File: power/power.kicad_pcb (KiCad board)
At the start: 2 copper layers, 75 x 56 mm, 24 parts, among them J1 GPIO, J2 PWM, J3 Conn_01x16, J4 JP_EXT, Q1 D15P05, U1 XL4015

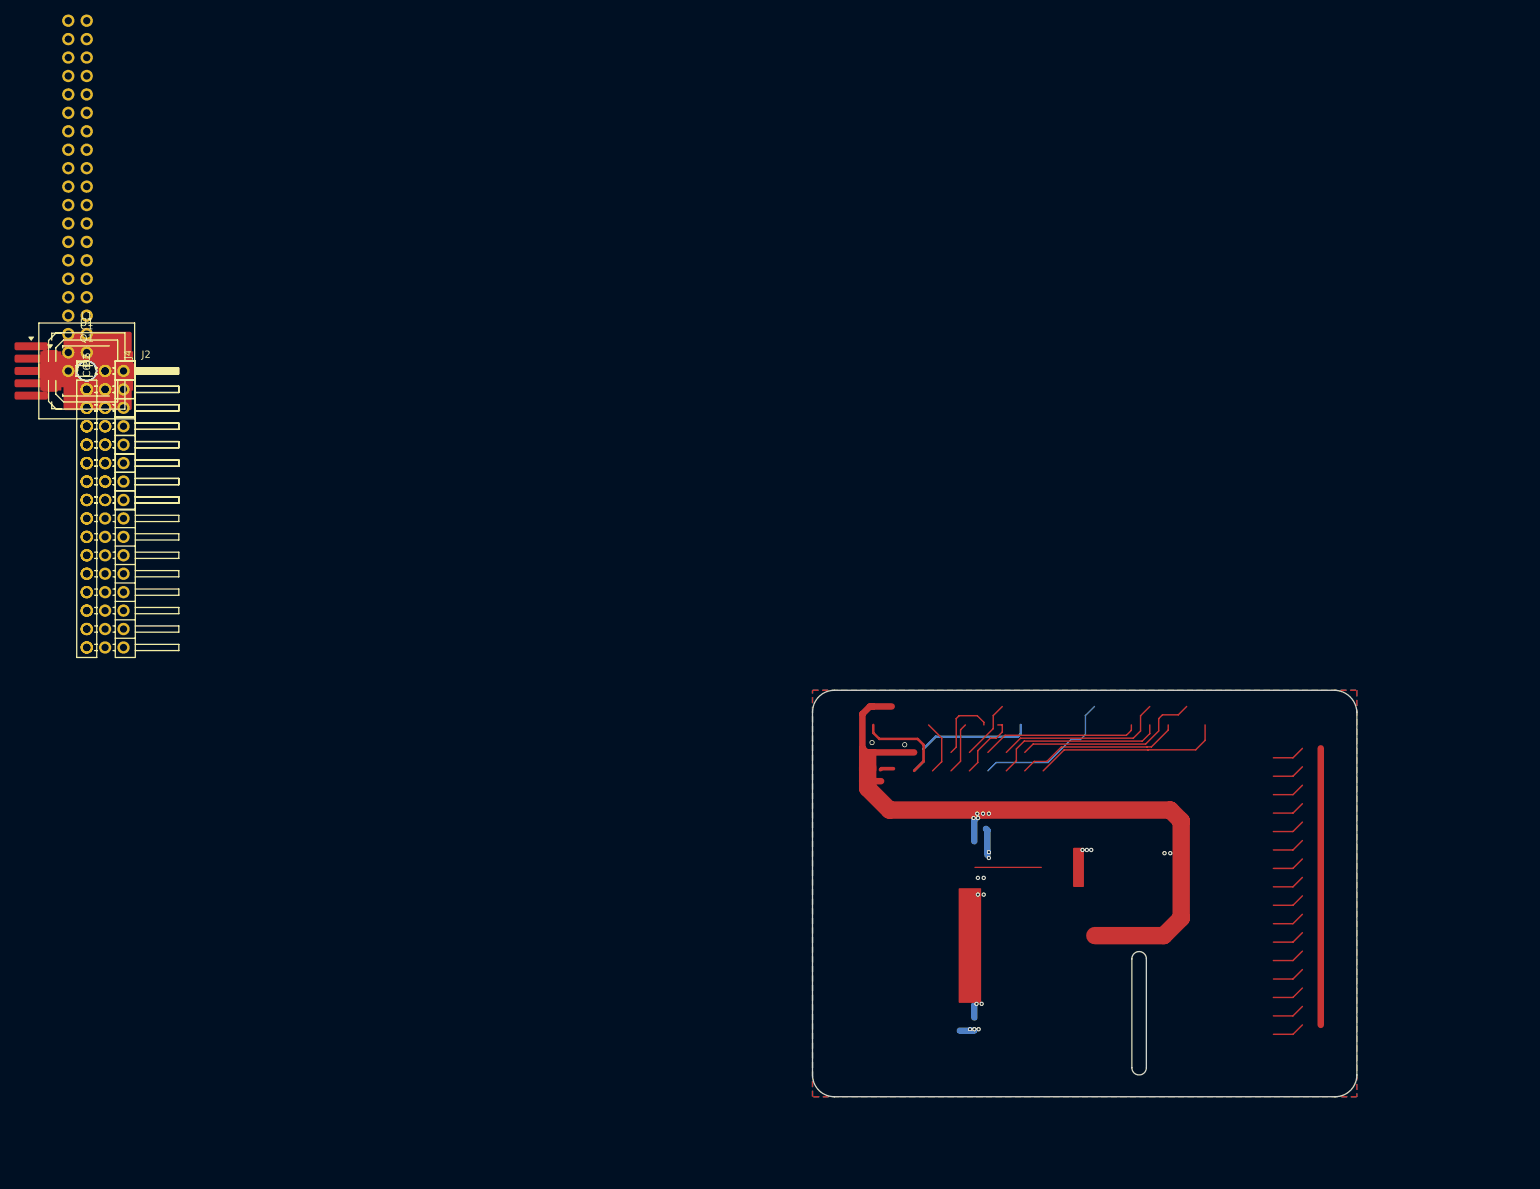
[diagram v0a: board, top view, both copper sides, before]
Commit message: manual downgrade to KiCAD 10.0
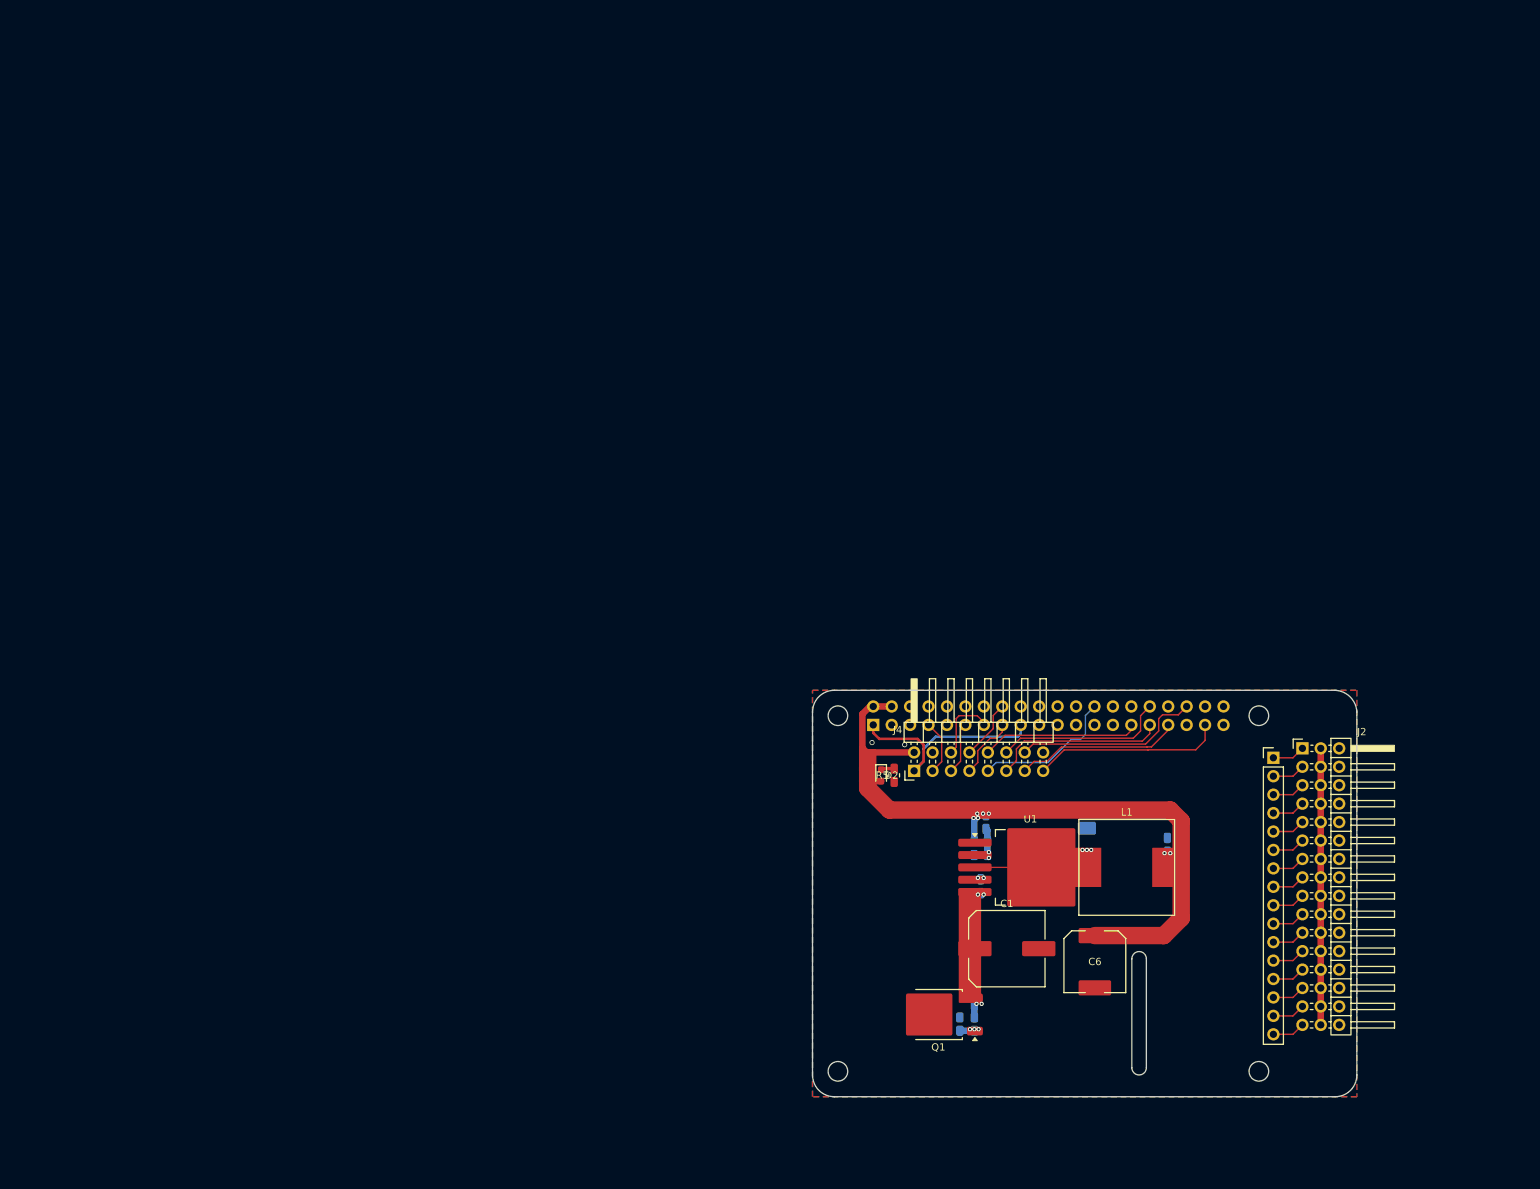
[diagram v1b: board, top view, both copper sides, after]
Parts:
- moved MH4 188.1 mm to (161.5, 96.5)
- moved J2 175.4 mm to (167.5, 52.0)
- moved J3 172.0 mm to (163.5, 53.3)
- moved MH2 168.3 mm to (161.5, 47.5)
- moved C4 162.6 mm to (148.9, 65.3), turned to 90 degrees
- moved C6 161.0 mm to (138.9, 81.4), turned to -90 degrees
- moved L1 158.8 mm to (143.3, 68.4)
- moved D1 152.4 mm to (137.8, 65.0), turned to 90 degrees
- moved R4 151.8 mm to (122.3, 90.0), turned to -90 degrees
- moved R3 150.2 mm to (120.3, 90.0), turned to 90 degrees
- moved C2 149.7 mm to (122.3, 86.4), turned to 90 degrees
- moved C1 149.7 mm to (126.8, 79.6)
- moved Q1 147.1 mm to (117.3, 88.7), turned to 180 degrees
- moved U1 146.9 mm to (130.0, 68.4)
- moved C3 142.2 mm to (123.2, 71.0), turned to 90 degrees
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
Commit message: move buzzer to power board
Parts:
- added BZ1: Buzzer, Buzzer_Beeper:MagneticBuzzer_PUI_AT-0927-TT-6-R, F.Cu at (188.3, 52.2)
- added D3: 1N4148W, Diode_SMD:D_SOD-123, F.Cu at (187.9, 59.1)
- added Q2: SS8050, Package_TO_SOT_SMD:SOT-23, F.Cu at (193.2, 59.7)
- added R6: 1KΩ (1001) ±1%, Resistor_SMD:R_0402_1005Metric, F.Cu at (197.0, 47.9)

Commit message: add buzzer bridged with jumper
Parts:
- added JP1: JP_BUZZ_PWM, Connector_PinHeader_2.54mm:PinHeader_1x02_P2.54mm_Vertical, F.Cu at (153.2, 53.4)
- moved BZ1 51.8 mm to (136.6, 55.6)
- moved Q2 46.7 mm to (146.8, 54.7), turned to 180 degrees
- moved R6 45.4 mm to (152.3, 55.8)
- moved D3 43.3 mm to (144.6, 57.8), turned to 90 degrees
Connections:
- R6 pad 2: /GPIO12/PWM0 -> /Buzzer/PWM
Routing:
- net /GPIO12/PWM0: track 23.6 -> 32.5 mm
- net Net-(BZ1--): track 0.00 -> 6.09 mm
- net +5V: track 97.5 -> 102.5 mm
- net Net-(Q2-B): track 0.00 -> 4.11 mm
- net /Buzzer/PWM: track 0.00 -> 2.56 mm

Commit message: rotate resistor
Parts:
- turned R2 to 180 degrees
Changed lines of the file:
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@@
 	(footprint "Resistor_SMD:R_0805_2012Metric"
 		(layer "B.Cu")
-		(at 123.1875 66.7)
+		(at 123.1875 66.7 180)
 		(descr "Resistor SMD 0805 (2012 Metric), square (rectangular) end terminal, IPC-7351 nominal, (Body size source: IPC-SM-782 page 72, https://www.pcb-3d.com/wordpress/wp-content/uploads/ipc-sm-782a_amendment_1_and_2.pdf)")
 		(tags "resistor")
 		(property "Reference" "R2"
-			(at 0 1.65 180)
+			(at 0 1.65 0)
 			(layer "B.SilkS")
 			(effects
@@
 		)
 		(property "Value" "3.3KΩ (3301) ±1%"
-			(at 5.5875 0 180)
+			(at 5.5875 0 0)
 			(layer "B.Fab")
 			(effects
@@
 		)
 		(property "Datasheet" ""
-			(at 0 0 180)
+			(at 0 0 0)
 			(layer "B.Fab")
 			(hide yes)
@@
 		)
 		(property "Description" "Resistor"
-			(at 0 0 180)
+			(at 0 0 0)
 			(layer "B.Fab")
 			(hide yes)
@@
 		(duplicate_pad_numbers_are_jumpers no)
 		(fp_line
+			(start -0.227064 0.735)
+			(end 0.227064 0.735)
+			(stroke
+				(width 0.12)
+				(type solid)
+			)
+			(layer "B.SilkS")
+		)
+		(fp_line
 			(start -0.227064 -0.735)
 			(end 0.227064 -0.735)
-			(stroke
-				(width 0.12)
-				(type solid)
-			)
-			(layer "B.SilkS")
-		)
-		(fp_line
-			(start -0.227064 0.735)
-			(end 0.227064 0.735)
 			(stroke
 				(width 0.12)
@@
 		)
 		(pad "1" smd roundrect
-			(at -0.9125 0 180)
+			(at -0.9125 0)
 			(size 1.025 1.4)
 			(layers "B.Cu" "B.Mask" "B.Paste")
@@
 		)
 		(pad "2" smd roundrect
-			(at 0.9125 0 180)
+			(at 0.9125 0)
 			(size 1.025 1.4)
 			(layers "B.Cu" "B.Mask" "B.Paste")
@@
 	)
 	(segment
-		(start 126.7 52.56)
-		(end 128.66 50.6)
-		(width 0.2)
-		(layer "F.Cu")
-		(net "/GPIO12{slash}PWM0")
-	)
-	(segment
-		(start 145.2 49.6)
-		(end 145.2 47.5)
-		(width 0.2)
-		(layer "F.Cu")
-		(net "/GPIO12{slash}PWM0")
-	)
-	(segment
-		(start 144.2 50.6)
-		(end 145.2 49.6)
-		(width 0.2)
-		(layer "F.Cu")
-		(net "/GPIO12{slash}PWM0")
-	)
-	(segment
-		(start 145.2 47.5)
-		(end 146.47 46.23)
-		(width 0.2)
-		(layer "F.Cu")
-		(net "/GPIO12{slash}PWM0")
-	)
-	(segment
-		(start 128.66 50.6)
-		(end 144.2 50.6)
-		(width 0.2)
-		(layer "F.Cu")
-		(net "/GPIO12{slash}PWM0")
-	)
-	(segment
-		(start 147.7 47.46)
-		(end 147.7 50.44)
-		(width 0.2)
-		(layer "B.Cu")
-		(net "/GPIO12{slash}PWM0")
-	)
-	(segment
-		(start 146.47 46.23)
-		(end 147.7 47.46)
-		(width 0.2)
-		(layer "B.Cu")
-		(net "/GPIO12{slash}PWM0")
-	)
-	(segment
-		(start 147.7 50.44)
-		(end 150.66 53.4)
-		(width 0.2)
-		(layer "B.Cu")
-		(net "/GPIO12{slash}PWM0")
+		(start 153.2 55.41)
+		(end 153.2 53.4)
+		(width 0.2)
+		(layer "F.Cu")
+		(net "/Buzzer/PWM")
+	)
+	(segment
+		(start 152.81 55.8)
+		(end 153.2 55.41)
+		(width 0.2)
+		(layer "F.Cu")
+		(net "/Buzzer/PWM")
 	)
 	(segment
@@
 		(layer "F.Cu")
 		(net "/GPIO6")
+	)
+	(segment
+		(start 126.7 52.56)
+		(end 128.66 50.6)
+		(width 0.2)
+		(layer "F.Cu")
+		(net "/GPIO12{slash}PWM0")
+	)
+	(segment
+		(start 145.2 49.6)
+		(end 145.2 47.5)
+		(width 0.2)
+		(layer "F.Cu")
+		(net "/GPIO12{slash}PWM0")
+	)
+	(segment
+		(start 144.2 50.6)
+		(end 145.2 49.6)
+		(width 0.2)
+		(layer "F.Cu")
+		(net "/GPIO12{slash}PWM0")
+	)
+	(segment
+		(start 145.2 47.5)
+		(end 146.47 46.23)
+		(width 0.2)
+		(layer "F.Cu")
+		(net "/GPIO12{slash}PWM0")
+	)
+	(segment
+		(start 128.66 50.6)
+		(end 144.2 50.6)
+		(width 0.2)
+		(layer "F.Cu")
+		(net "/GPIO12{slash}PWM0")
+	)
+	(segment
+		(start 147.7 47.46)
+		(end 147.7 50.44)
+		(width 0.2)
+		(layer "B.Cu")
+		(net "/GPIO12{slash}PWM0")
+	)
+	(segment
+		(start 146.47 46.23)
+		(end 147.7 47.46)
+		(width 0.2)
+		(layer "B.Cu")
+		(net "/GPIO12{slash}PWM0")
+	)
+	(segment
+		(start 147.7 50.44)
+		(end 150.66 53.4)
+		(width 0.2)
+		(layer "B.Cu")
+		(net "/GPIO12{slash}PWM0")
 	)
 	(segment
@@
 		(net "Net-(D2-K)")
 	)
-	(segment
-		(start 153.2 55.41)
-		(end 153.2 53.4)
-		(width 0.2)
-		(layer "F.Cu")
-		(net "/Buzzer/PWM")
-	)
-	(segment
-		(start 152.81 55.8)
-		(end 153.2 55.41)
-		(width 0.2)
-		(layer "F.Cu")
-		(net "/Buzzer/PWM")
-	)
 	(zone

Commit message: update footprints from library
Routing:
- net /GPIO13/PWM1: track 22.8 -> 22.1 mm
- net /GPIO22: track 9.30 -> 8.68 mm

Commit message: lots of changes
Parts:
- added C10: 1.0uF (105) 10% 25V, Capacitor_SMD:C_0402_1005Metric, F.Cu at (125.5, 88.5)
- added C11: 330nF (334) 10% 50V, Capacitor_SMD:C_0805_2012Metric, F.Cu at (118.3, 94.7)
- added C12: 100nF(104) 10% 50V, Capacitor_SMD:C_0805_2012Metric, F.Cu at (122.4, 91.7)
- added C7: 1.0uF (105) 10% 25V, Capacitor_SMD:C_0402_1005Metric, F.Cu at (119.6, 86.5)
- added C8: 22uF (226) 20% 6.3V, Capacitor_SMD:C_0603_1608Metric, F.Cu at (113.8, 92.5)
- added C9: 100nF (104) 10% 16V, Capacitor_SMD:C_0402_1005Metric, F.Cu at (126.5, 88.5)
- added J5: JP_VOLTS, Connector_PinSocket_2.54mm:PinSocket_1x02_P2.54mm_Vertical, B.Cu at (114.6, 90.0)
- added R7: 1KΩ (1001) ±1%, Resistor_SMD:R_0805_2012Metric, F.Cu at (112.5, 84.5)
- added R8: 4.7KΩ (4701) ±1%, Resistor_SMD:R_0805_2012Metric, F.Cu at (116.0, 84.5)
- added U2: REF5050IDGK, Package_SO:VSSOP-8_3x3mm_P0.65mm, F.Cu at (121.9, 88.8)
- added U3: L78L06_SOT89, Package_TO_SOT_SMD:SOT-89-3, F.Cu at (121.8, 95.7)
- C2, C3, C4, C5, D1, R1, R2, R3, R4: moved to F.Cu
- J2: value PWM -> PWM_OUT
- J3: value Conn_01x16 -> PWM_IN; footprint Connector_PinHeader_2.54mm:PinHeader_1x16_P2.54mm_Vertical -> Connector_PinSocket_2.54mm:PinSocket_1x16_P2.54mm_Vertical; moved to B.Cu
- J4: footprint Connector_PinHeader_2.54mm:PinHeader_2x08_P2.54mm_Horizontal -> Connector_PinHeader_2.54mm:PinHeader_2x08_P2.54mm_Vertical
- moved D1 22.8 mm to (115.9, 71.2), turned to -90 degrees
- moved C4 17.1 mm to (135.6, 76.0), turned to 180 degrees
- moved C2 11.6 mm to (119.5, 75.1), turned to 180 degrees
- moved Q1 9.67 mm to (113.0, 80.0)
- moved R1 6.86 mm to (116.9, 62.1), turned to -90 degrees
- moved R4 6.25 mm to (119.3, 84.5), turned to 0 degrees
- moved R6 5.89 mm to (146.5, 56.8), turned to -90 degrees
- moved C5 5.06 mm to (118.8, 62.0)
- moved JP1 4.93 mm to (149.0, 56.0), turned to 180 degrees
- moved R3 4.65 mm to (122.7, 86.0), turned to 0 degrees
- moved C3 4.49 mm to (118.7, 71.0)
- moved R2 4.48 mm to (118.8, 65.8), turned to 90 degrees
- moved Q2 1.67 mm to (145.3, 54.0)
- moved D3 0.40 mm to (144.6, 58.2)
- moved L1 0.10 mm to (143.3, 68.3)
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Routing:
- net /VIN: track 1.74 -> 29.6 mm, vias 4 -> 8
- net +5V: track 102.1 -> 82.0 mm, vias 7 -> 0
- net +6V: track 0.00 -> 9.70 mm
- net /VREF: track 0.00 -> 8.89 mm
- net /GPIO14/TXD0: track 0.00 -> 7.63 mm
- net Net-(D1-K): track 9.15 -> 16.3 mm, vias 3 -> 0
- net /BATT_VDIV: track 0.00 -> 4.57 mm
- net Net-(Q1-G): track 1.99 -> 5.83 mm, vias 3 -> 0
- net Net-(U1-VC): track 0.00 -> 3.70 mm, vias 2 -> 0
- net Net-(U1-FB): track 3.68 -> 0.02 mm, vias 2 -> 10
- net Net-(Q2-B): track 3.90 -> 1.42 mm
- net /GPIO7/SPI0.CE1: track 19.9 -> 21.0 mm
- net Net-(U2-Trim/NR): track 0.00 -> 1.04 mm
- net Net-(BZ1--): track 5.69 -> 6.61 mm
- net /GPIO12/PWM0: track 32.5 -> 31.9 mm
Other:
- board text added: "+"
- board text added: "-"
- board text added: "BATT_VDIV"
- board text added: "PWM0"
- board text added: "PWM15"
- board text added: "VREF"
- board text added: "closed = Buzzer open = PWM0"

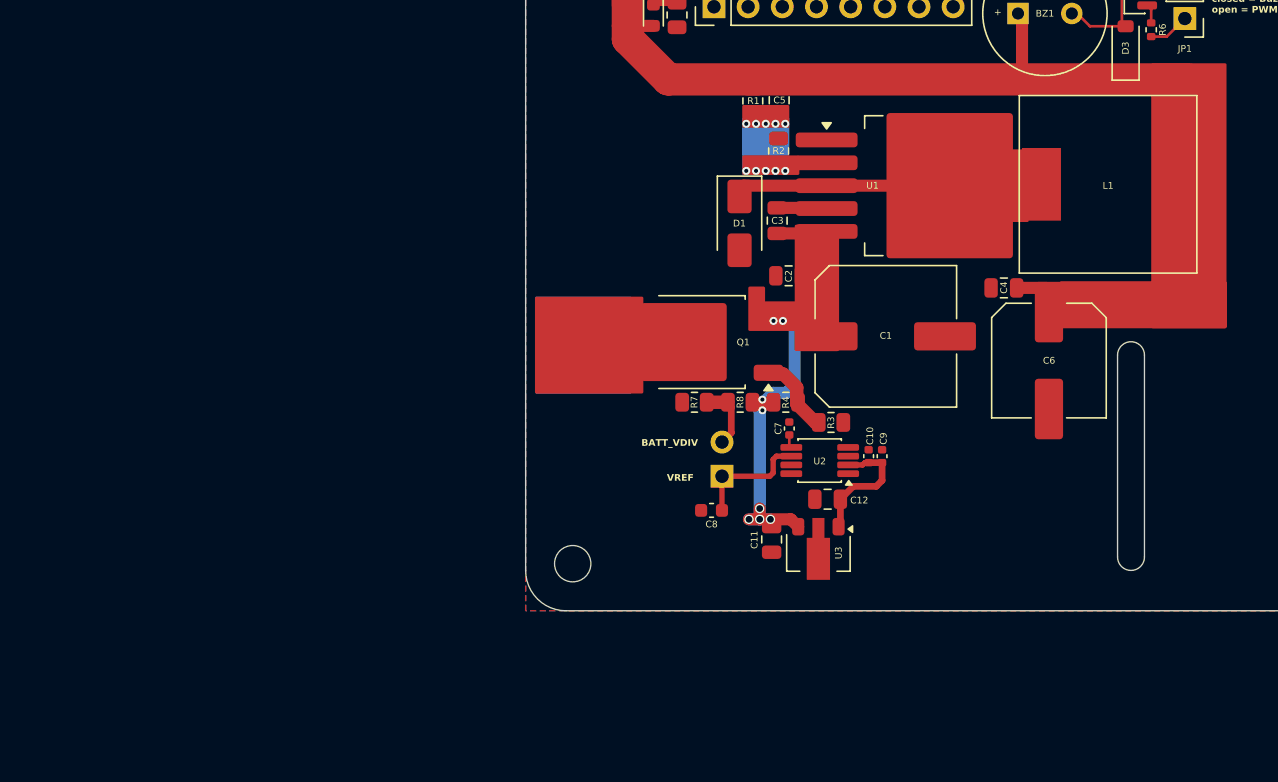
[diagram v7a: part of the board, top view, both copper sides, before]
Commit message: initial TPS56A37 DCDC attempt
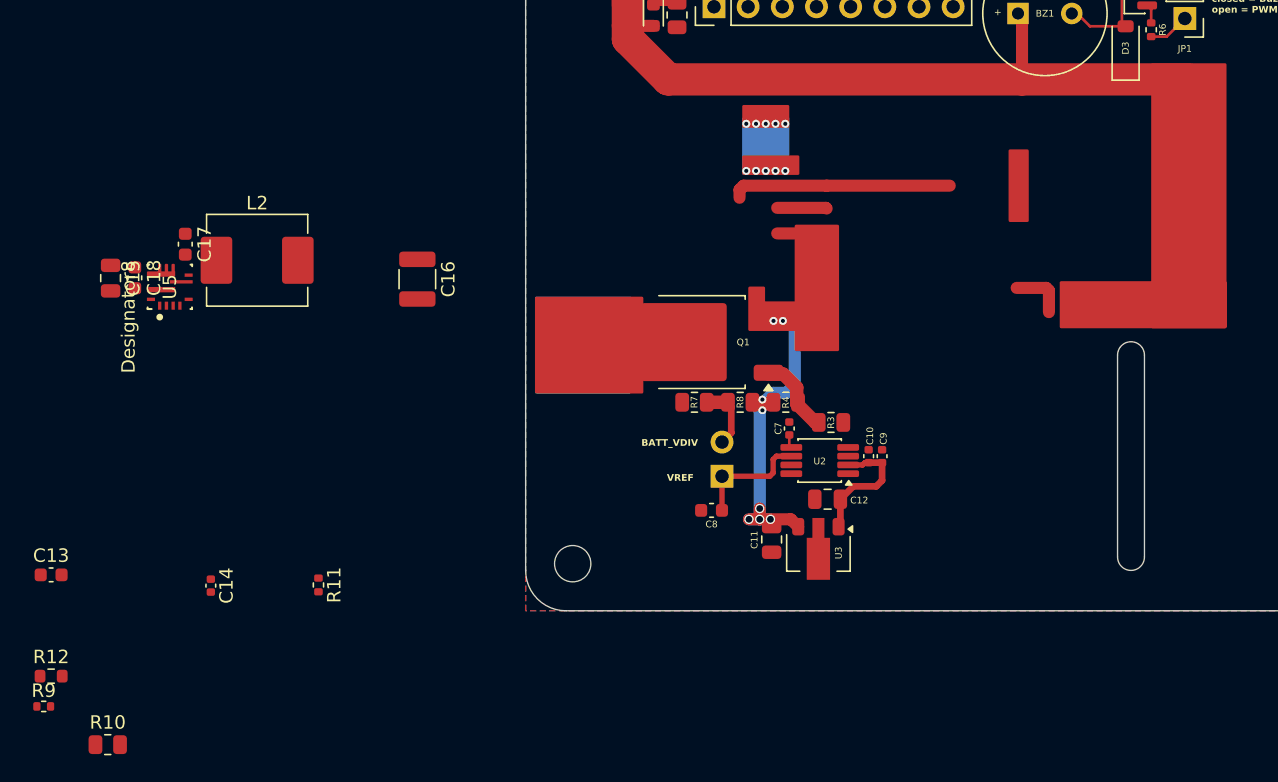
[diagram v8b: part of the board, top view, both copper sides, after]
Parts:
- removed C1: 220uF/50V, Capacitor_SMD:C_Elec_10x10.2
- removed C2, C3, C4: 1uF (105) 10% 50V, Capacitor_SMD:C_0805_2012Metric
- removed C5: 33nF (333) 10% 50V, Capacitor_SMD:C_0805_2012Metric
- removed C6: 470uF/16V, Capacitor_SMD:C_Elec_8x10.2
- removed D1: SS54, Diode_SMD:D_SMA
- removed L1: 47uH, Inductor_SMD:L_Neosid_SM-NE127
- removed R1: 10KΩ (1002) ±1%, Resistor_SMD:R_0805_2012Metric
- removed R2: 3.3KΩ (3301) ±1%, Resistor_SMD:R_0805_2012Metric
- removed U1: XL4015, Package_TO_SOT_SMD:TO-263-5_TabPin3
- added C13: 150pF / 25V, Capacitor_SMD:C_0603_1608Metric, F.Cu at (64.7, 97.3)
- added C14: 22nF (105) 10% 16V, Capacitor_SMD:C_0402_1005Metric, F.Cu at (76.6, 98.1)
- added C15: 10uF 10% 35V, Capacitor_SMD:C_0805_2012Metric, F.Cu at (69.1, 75.3)
- added C16: 22uF 10% 16V, Capacitor_SMD:C_1210_3225Metric, F.Cu at (92.0, 75.3)
- added C17: 100nF / 16V, Capacitor_SMD:C_0603_1608Metric, F.Cu at (74.7, 72.8)
- added C18: 1uF (105) 10% 35V, Capacitor_SMD:C_0603_1608Metric, F.Cu at (71.0, 75.2)
- added L2: 3.3uH 16A 6.5mΩ ±20%, Inductor_SMD:L_Chilisin_BMRB00060612, F.Cu at (80.0, 73.9)
- added R10: 72.2KΩ ±1%, Resistor_SMD:R_0805_2012Metric, F.Cu at (68.9, 110.0)
- added R11: 52.3KΩ ±1%, Resistor_SMD:R_0402_1005Metric, F.Cu at (84.6, 98.1)
- added R12: 100kΩ / 1%, Resistor_SMD:R_0603_1608Metric, F.Cu at (64.7, 104.9)
- added R9: 10KΩ (1001) ±1%, Resistor_SMD:R_0402_1005Metric, F.Cu at (64.2, 107.1)
- added U5: TPS56A37RPAR, pilotpi:RPA0010A-MFG, F.Cu at (73.5, 75.9)
- D2: value LED -> LED_RED
- Q2: value SS8050 -> BC847C
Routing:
- net (no net): track 0.00 -> 20.1 mm, vias 0 -> 10
- net Net-(D1-K): track 16.3 -> 0.00 mm
- net Net-(U1-VC): track 3.70 -> 0.00 mm
- net Net-(U1-FB): track 0.02 -> 0.00 mm, vias 10 -> 0
